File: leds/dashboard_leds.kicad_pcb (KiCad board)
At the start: 2 copper layers, 21 x 76.6 mm, 38 parts, among them J1 Harness, J2 Buttons, J3 Expansion Connector, Q1 2N7002, Q2 2N7002, Q3 2N7002, U1 74LVC3G17, U2 AL5809, U3 AL5809, U4 AL5809, U5 AL5809, U6 AL5809

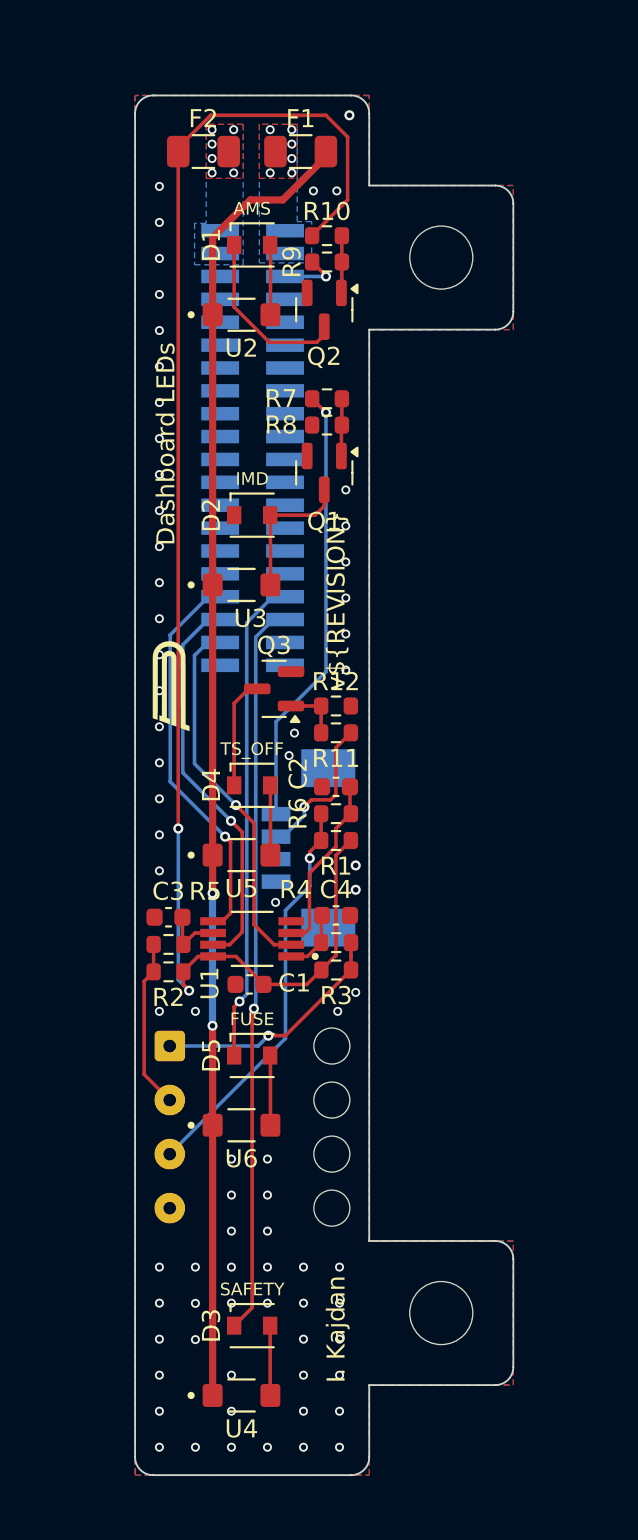
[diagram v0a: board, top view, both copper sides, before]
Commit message: Fix connector wiring
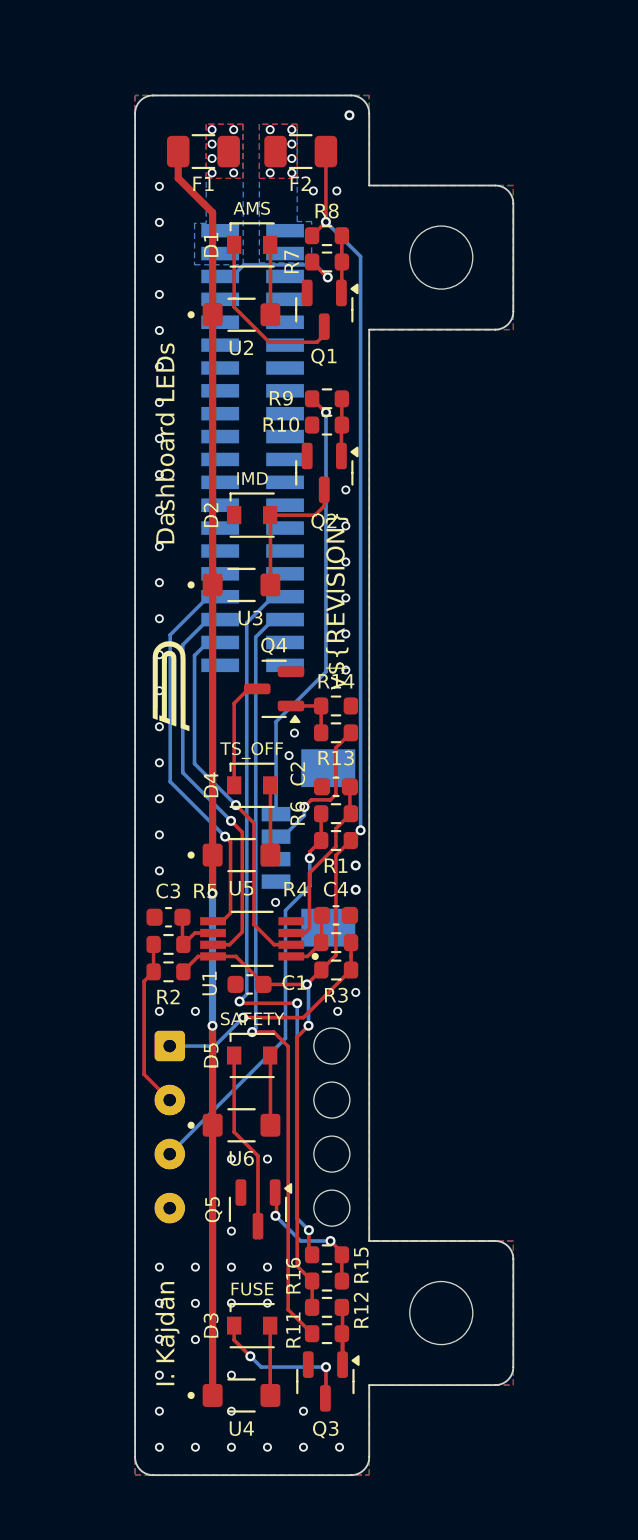
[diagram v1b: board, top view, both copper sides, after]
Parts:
- added Q3: 2N7002, Package_TO_SOT_SMD:SOT-23, F.Cu at (155.6, 134.8)
- added Q5: 2N7002, Package_TO_SOT_SMD:SOT-23, F.Cu at (151.8, 125.2)
- added R11: 100R, Resistor_SMD:R_0603_1608Metric, F.Cu at (155.7, 132.1)
- added R12: 10k, Resistor_SMD:R_0603_1608Metric, F.Cu at (155.7, 130.7)
- added R15: 100R, Resistor_SMD:R_0603_1608Metric, F.Cu at (155.7, 127.8)
- added R16: 10k, Resistor_SMD:R_0603_1608Metric, F.Cu at (155.7, 129.2)
- moved F1 5.40 mm to (148.8, 66.5), turned to 180 degrees
- moved F2 5.40 mm to (154.2, 66.5), turned to 180 degrees
- renumbered Q2 to Q1, Q1 to Q2, Q3 to Q4, R8 to R10, R11 to R13, R12 to R14, R9 to R7, R10 to R8, R7 to R9
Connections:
- D3 pad 1: /SAFETY -> Net-(D3-K)
- D5 pad 1: /FUSE -> Net-(D5-K)
- F1 pad 1: Net-(J3-Pin_2) -> Net-(J3-Pin_1)
- F2 pad 2: Net-(J3-Pin_1) -> Net-(J3-Pin_2)
- J3 pad 34: /FUSE -> /SAFETY
- J3 pad 36: /SAFETY -> /FUSE
- J3 pad 5: GND -> /AMS
- J3 pad 6: /AMS -> GND
- J3 pad 7: unconnected-(J3-Pin_7-Pad7) -> GND
- J3 pad 8: GND -> unconnected-(J3-Pin_8-Pad8)
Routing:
- net /FUSE: track 27.0 -> 42.9 mm
- net Net-(D5-K): track 0.00 -> 10.0 mm
- net Net-(D3-K): track 0.00 -> 8.27 mm, vias 0 -> 2
- net Net-(Q5-G): track 0.00 -> 7.44 mm, vias 0 -> 2
- net +3.3V: track 82.1 -> 75.8 mm, vias 2 -> 4
- net Net-(Q3-G): track 0.00 -> 4.93 mm
- net /AMS: track 3.40 -> 7.75 mm
- net +5V: track 72.7 -> 70.1 mm
- net /SAFETY: track 40.8 -> 41.5 mm, vias 1 -> 3
- net GND: vias 74 -> 62

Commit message: Update button labels
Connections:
- net /BTN1 renamed /TSA_BTN
- net /BTN1_RC renamed /TSA_BTN_RC
- net /BTN2 renamed /USR_BTN
- net /BTN2_RC renamed /USR_BTN_RC
- net /FUSE renamed /FUSE_LED
- net /RTD renamed /RTD_BTN
- net /SAFETY renamed /SAFETY_LED

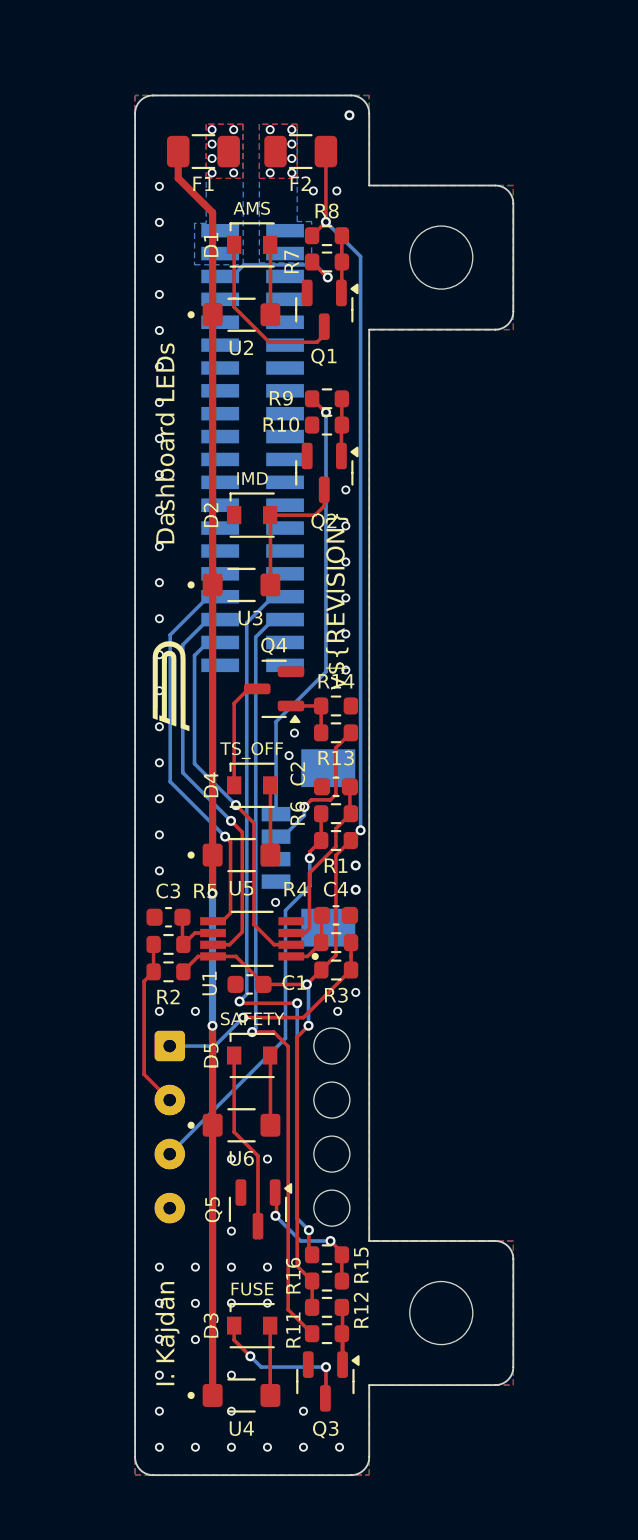
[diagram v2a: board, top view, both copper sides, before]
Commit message: Edit PCB layout
*without zone
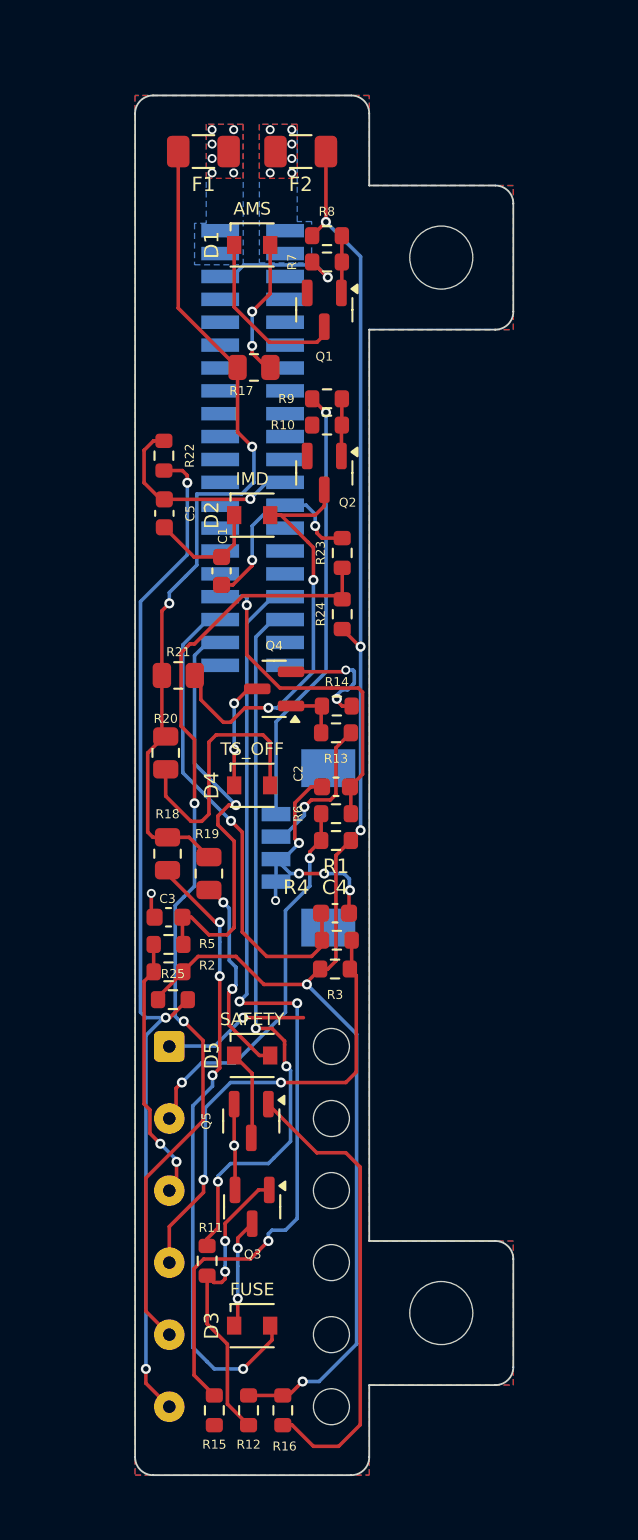
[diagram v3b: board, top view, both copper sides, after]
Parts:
- removed U1: 74LVC3G17, Local_Library:74LVC3G17
- removed U2, U3, U4, U5, U6: AL5809, Local_Library:AL5809-20QP1-7
- added C5: 1u, Capacitor_SMD:C_0603_1608Metric, F.Cu at (146.6, 86.6)
- added R17: 140, Resistor_SMD:R_0805_2012Metric, F.Cu at (151.6, 78.5)
- added R18: 140, Resistor_SMD:R_0805_2012Metric, F.Cu at (146.8, 105.5)
- added R19: 140, Resistor_SMD:R_0805_2012Metric, F.Cu at (149.1, 106.6)
- added R20: 140, Resistor_SMD:R_0805_2012Metric, F.Cu at (146.7, 99.9)
- added R21: 140, Resistor_SMD:R_0805_2012Metric, F.Cu at (147.4, 95.6)
- added R22: 1k, Resistor_SMD:R_0603_1608Metric, F.Cu at (146.6, 83.4)
- added R23: 1k, Resistor_SMD:R_0603_1608Metric, F.Cu at (156.5, 88.8)
- added R24: 10k, Resistor_SMD:R_0603_1608Metric, F.Cu at (156.5, 92.2)
- added R25: 10k, Resistor_SMD:R_0603_1608Metric, F.Cu at (147.1, 113.6)
- C1, C2, C3, C4: value 100n -> 1u
- G***: moved to B.Cu
- J2: value Buttons -> Conn_01x06; footprint Local_Library:SolderWire-0.15sqmm_Relief -> Connector_Wire:SolderWire-0.15sqmm_1x06_P4mm_D0.5mm_OD1.5mm_Relief
- moved G*** 30.2 mm to (151.8, 66.4), turned to 180 degrees
- moved C1 23.0 mm to (149.8, 89.8), turned to 90 degrees
- moved R15 10.7 mm to (149.4, 136.4), turned to -90 degrees
- moved Q3 10.5 mm to (151.5, 125.1)
- moved R11 7.79 mm to (149.0, 128.1), turned to -90 degrees
- moved R16 7.58 mm to (153.2, 136.4), turned to -90 degrees
- moved R12 7.19 mm to (151.3, 136.4), turned to -90 degrees
- moved Q5 4.92 mm to (151.4, 120.3)
- moved R4 0.14 mm to (156.2, 110.3)
- moved C4 0.14 mm to (156.1, 108.8)
- moved R3 0.09 mm to (156.1, 111.9)
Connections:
- C1 pad 1: +3.3V -> /DRS_BTN
- C2 pad 1: /USR_BTN_RC -> /CS_BTN
- C3 pad 1: /TSA_BTN_RC -> /TSA_BTN
- C4 pad 1: /RTD_RC -> /RTD_BTN
- J2 pad 1: Net-(J2-Pin_1) -> GND
- J2 pad 4: GND -> Net-(J2-Pin_4)
- J3 pad 24: unconnected-(J3-Pin_24-Pad24) -> /USR_BTN
- J3 pad 26: unconnected-(J3-Pin_26-Pad26) -> /DRS_BTN
- J3 pad 33: /USR_BTN -> /CS_BTN
- R1 pad 2: Net-(J2-Pin_3) -> Net-(J2-Pin_2)
- R2 pad 2: Net-(J2-Pin_2) -> Net-(J2-Pin_3)
- R3 pad 2: Net-(J2-Pin_1) -> Net-(J2-Pin_4)
- R4 pad 1: /RTD_RC -> /RTD_BTN
- R4 pad 2: Net-(J2-Pin_1) -> Net-(J2-Pin_4)
- R5 pad 1: Net-(J2-Pin_2) -> Net-(J2-Pin_3)
- R5 pad 2: /TSA_BTN_RC -> /TSA_BTN
- R6 pad 1: /USR_BTN_RC -> /CS_BTN
- R6 pad 2: Net-(J2-Pin_3) -> Net-(J2-Pin_2)
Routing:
- net Net-(J2-Pin_6): track 0.00 -> 58.1 mm, vias 0 -> 3
- net Net-(J2-Pin_5): track 0.00 -> 53.4 mm, vias 0 -> 2
- net GND: track 0.00 -> 42.2 mm, vias 62 -> 10
- net Net-(D3-A): track 3.88 -> 35.0 mm, vias 0 -> 4
- net Net-(J2-Pin_4): track 0.00 -> 26.1 mm, vias 0 -> 2
- net +5V: track 70.1 -> 47.9 mm
- net /CS_BTN: track 0.00 -> 19.7 mm, vias 0 -> 1
- net Net-(Q5-G): track 7.44 -> 26.1 mm, vias 2 -> 0
- net Net-(D2-A): track 8.40 -> 23.9 mm, vias 0 -> 2
- net +3.3V: track 75.8 -> 89.4 mm, vias 4 -> 5
- net Net-(J2-Pin_1): track 13.3 -> 0.00 mm, vias 1 -> 0
- net /SAFETY_LED: track 41.5 -> 53.7 mm
- net Net-(J2-Pin_2): track 9.45 -> 21.5 mm, vias 0 -> 2
- net Net-(Q3-G): track 4.93 -> 16.8 mm, vias 0 -> 2
- net /DRS_BTN: track 0.00 -> 11.1 mm, vias 0 -> 2
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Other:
- board text added: "M. Błotniak"
- board text removed: "I. Kajdan"
- board text removed: "JLCJLCJLCJLC"
- board text removed: "v${REVISION}"

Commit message: Add zones and some changes
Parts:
- moved C3 5.75 mm to (152.6, 109.3), turned to 90 degrees
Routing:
- net GND: track 42.2 -> 63.2 mm, vias 10 -> 13
- net /TSA_BTN: track 23.8 -> 29.5 mm, vias 1 -> 3
- net Net-(Q5-G): track 26.1 -> 31.3 mm
- net Net-(J2-Pin_5): track 53.4 -> 52.9 mm
- added copper zone on B.Cu, net (none)
- added copper zone on F.Cu, net (none)

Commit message: Fixing bugs on PCB
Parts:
- moved R14 0.94 mm to (155.7, 98.1)
- moved R13 0.89 mm to (155.8, 99.6)
- moved R9 0.64 mm to (155.7, 79.6)
- moved Q4 0.42 mm to (152.3, 96.3)
- moved R2 0.25 mm to (147.1, 112.1)
- moved R5 0.15 mm to (147.0, 110.5)
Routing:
- net GND: track 63.2 -> 111.2 mm, vias 13 -> 26
- net Net-(J3-Pin_1): track 0.00 -> 3.40 mm
- net Net-(J3-Pin_2): track 0.00 -> 3.37 mm
- net +3.3V: track 89.4 -> 92.5 mm
- net Net-(J2-Pin_6): track 58.1 -> 56.9 mm
- net /TS_OFF: track 8.34 -> 7.27 mm
- net Net-(D1-A): track 7.78 -> 8.67 mm
- net /IMD: track 24.5 -> 25.2 mm
- net Net-(Q2-G): track 3.19 -> 3.83 mm

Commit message: Editing zones and minor changes
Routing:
- removed copper zone on B.Cu, net (none)
- removed copper zone on F.Cu, net (none)
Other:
- board text added: "v 2.0"

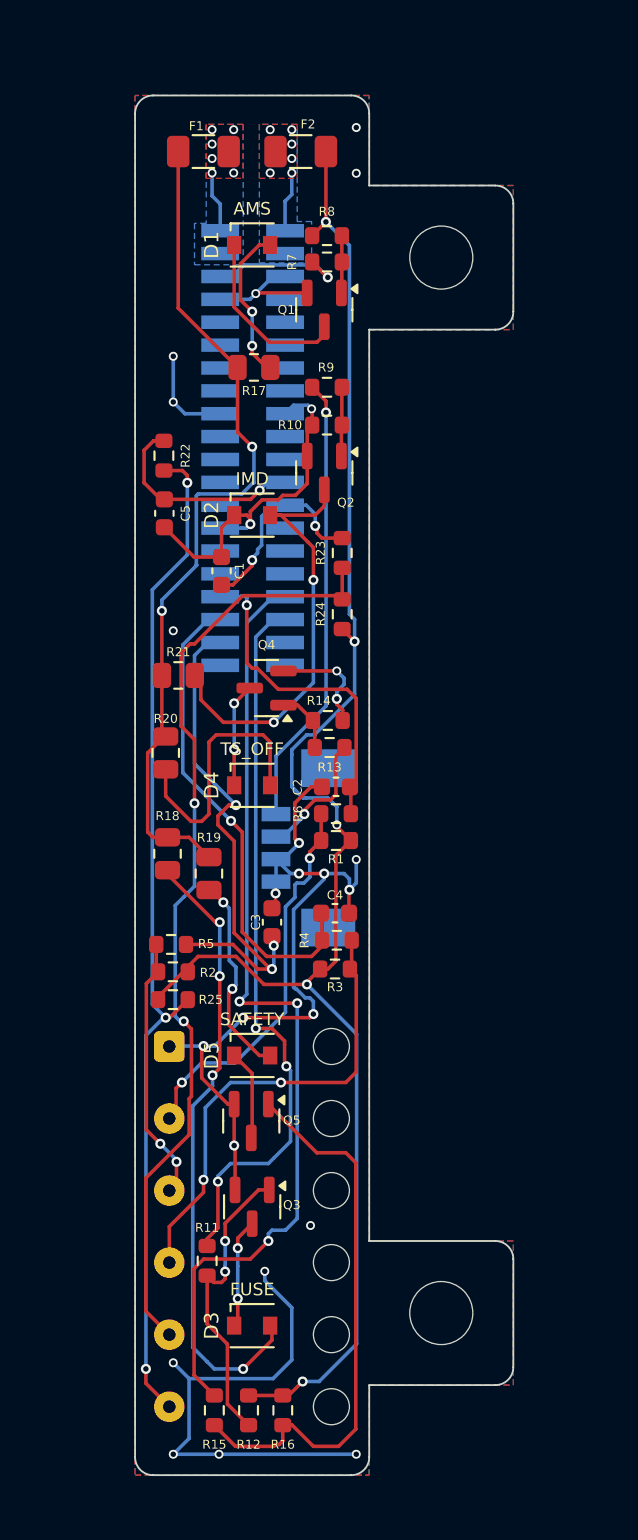
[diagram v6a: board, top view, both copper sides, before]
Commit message: Complete change of design
Change from 2 layer to 4 layer, add bigger resistors, change diodes
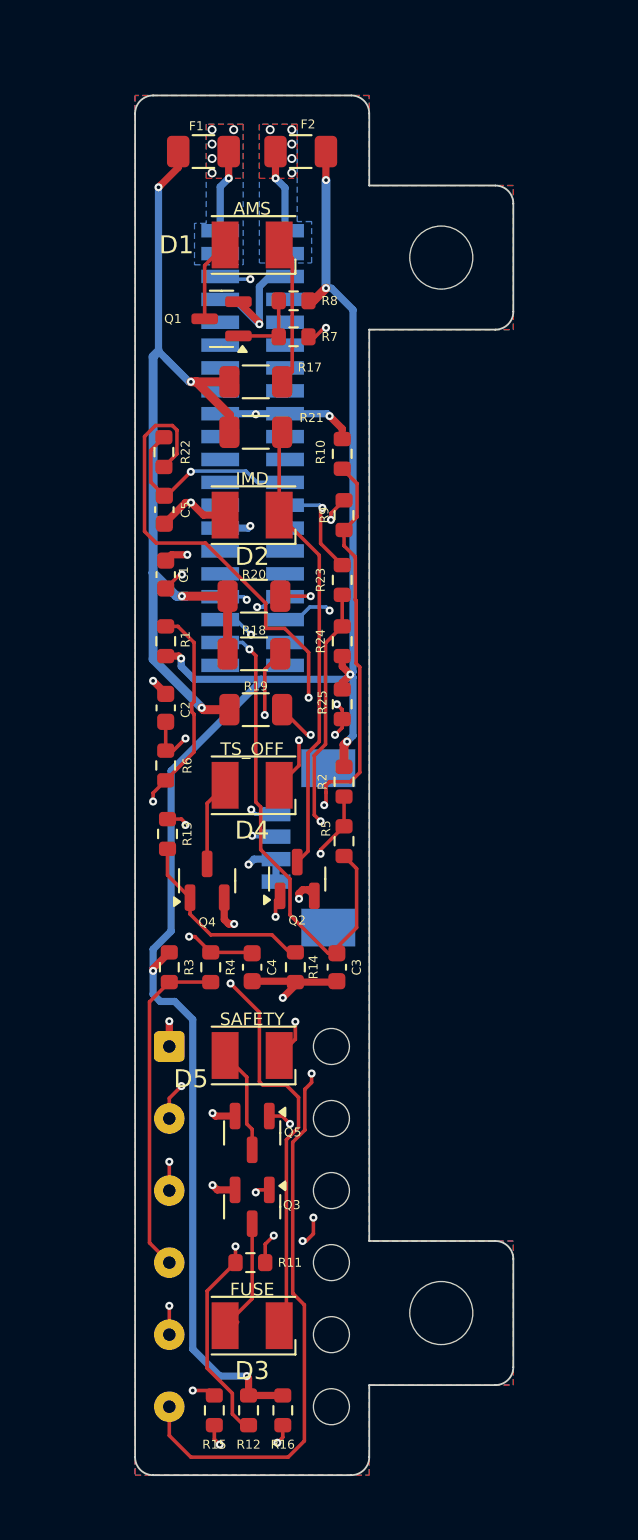
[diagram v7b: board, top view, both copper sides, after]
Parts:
- D1, D2, D3, D4, D5: footprint Local_Library:Wurth_Elektronik_150224 -> LED_SMD:LED_PLCC-2_3.4x3.0mm_AK
- Q1, Q2, Q3, Q4, Q5: value 2N7002 -> BSS138
- R17, R18, R19, R20, R21: value 140 -> 150; footprint Resistor_SMD:R_0805_2012Metric -> Resistor_SMD:R_1206_3216Metric
- moved Q2 22.6 mm to (154.0, 106.9), turned to 90 degrees
- moved R25 18.9 mm to (156.5, 97.2), turned to -90 degrees
- moved R1 14.6 mm to (146.7, 93.7), turned to 90 degrees
- moved R2 14.2 mm to (156.6, 101.5), turned to -90 degrees
- moved R21 14.2 mm to (151.7, 82.1)
- moved R14 13.8 mm to (153.9, 111.8), turned to -90 degrees
- moved R18 12.1 mm to (151.6, 94.4), turned to 0 degrees
- moved Q4 11.2 mm to (149.0, 107.0), turned to 90 degrees
- moved R5 11.2 mm to (156.6, 104.8), turned to -90 degrees
- moved C2 10.4 mm to (146.7, 97.4), turned to 90 degrees
- moved R13 10.2 mm to (146.8, 104.4), turned to -90 degrees
- moved R20 9.98 mm to (151.6, 91.2), turned to 0 degrees
- moved R6 9.83 mm to (146.7, 100.6), turned to -90 degrees
- moved R19 9.46 mm to (151.7, 97.5), turned to 0 degrees
- moved R3 9.20 mm to (146.9, 111.8), turned to -90 degrees
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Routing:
- net Net-(Q2-G): track 3.83 -> 30.9 mm, vias 0 -> 2
- net Net-(J2-Pin_6): track 56.9 -> 80.0 mm, vias 3 -> 4
- net Net-(J2-Pin_3): track 15.1 -> 29.0 mm
- net Net-(D5-A): track 11.4 -> 24.5 mm
- net Net-(J2-Pin_2): track 21.7 -> 31.5 mm
- net Net-(D3-A): track 35.0 -> 42.9 mm, vias 4 -> 2
- net Net-(J2-Pin_4): track 26.1 -> 18.8 mm, vias 2 -> 0
- net Net-(Q4-G): track 3.53 -> 10.9 mm
- net +3.3V: track 92.5 -> 99.3 mm, vias 5 -> 7
- net /DRS_BTN: track 11.1 -> 17.1 mm
- net Net-(D1-K): track 9.89 -> 4.57 mm
- net /CS_BTN: track 19.2 -> 14.3 mm, vias 1 -> 2
- net +5V: track 47.9 -> 52.7 mm, vias 2 -> 4
- net Net-(Q5-G): track 31.1 -> 26.3 mm, vias 0 -> 3
- net GND: track 111.2 -> 115.7 mm, vias 26 -> 14
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- added copper zone on In1.Cu, net GND
- added copper zone on In2.Cu, net GND
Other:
- copper layers 2 -> 4

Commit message: Changing the path guidance
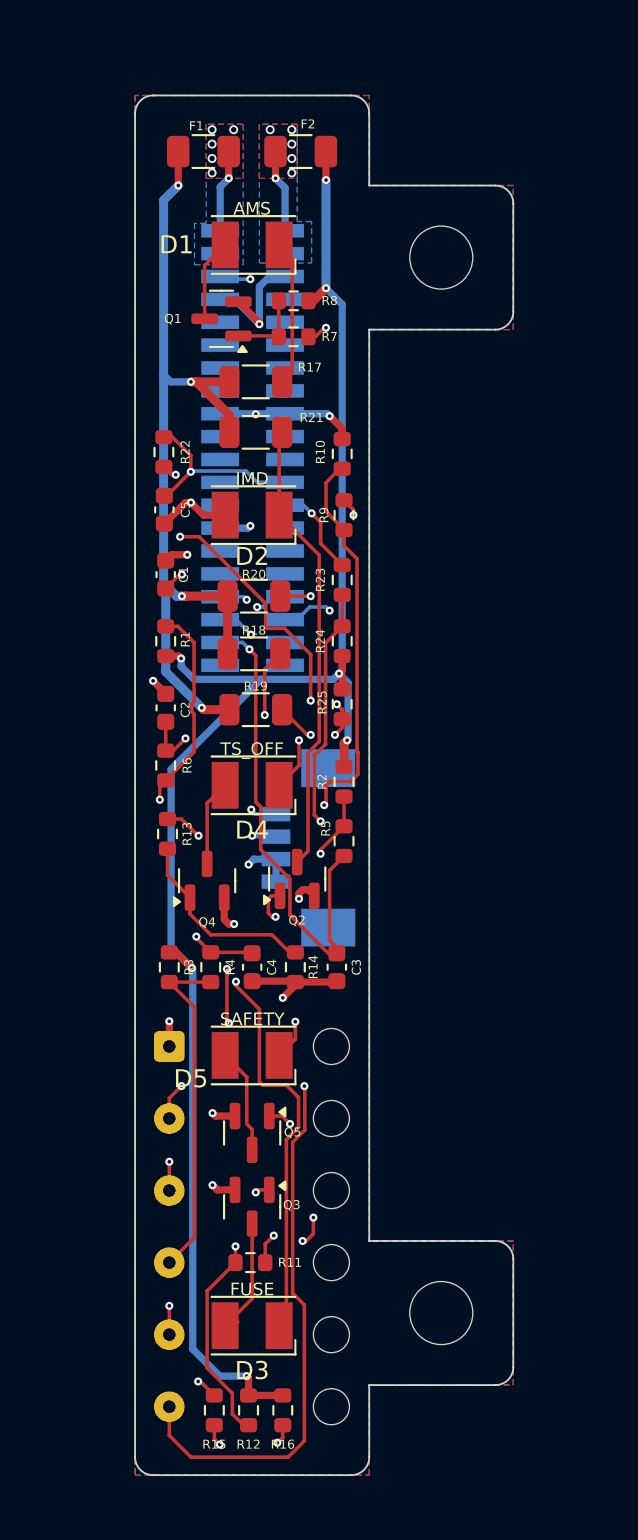
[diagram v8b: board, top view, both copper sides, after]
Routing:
- net Net-(J2-Pin_6): track 80.0 -> 72.3 mm, vias 4 -> 6
- net +5V: track 52.7 -> 48.5 mm
- net +3.3V: track 99.3 -> 97.0 mm
- net /SAFETY_LED: track 53.4 -> 52.1 mm, vias 2 -> 4
- net /RTD_BTN: track 26.3 -> 24.9 mm
- net /DRS_BTN: track 17.1 -> 15.9 mm
- net /USR_BTN: track 14.2 -> 13.1 mm
